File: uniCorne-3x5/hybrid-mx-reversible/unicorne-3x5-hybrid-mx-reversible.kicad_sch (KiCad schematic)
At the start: 87 parts, among them J1 MJ-4PP-9, J2 Nice!View, J3 Conn_01x02, J3 Conn_01x03, SW1 SW_MX_HS, SW10 SW_MX_HS, SW11 SW_MX_HS, SW12 SW_MX_HS, SW13 SW_MX_HS, SW14 SW_MX_HS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

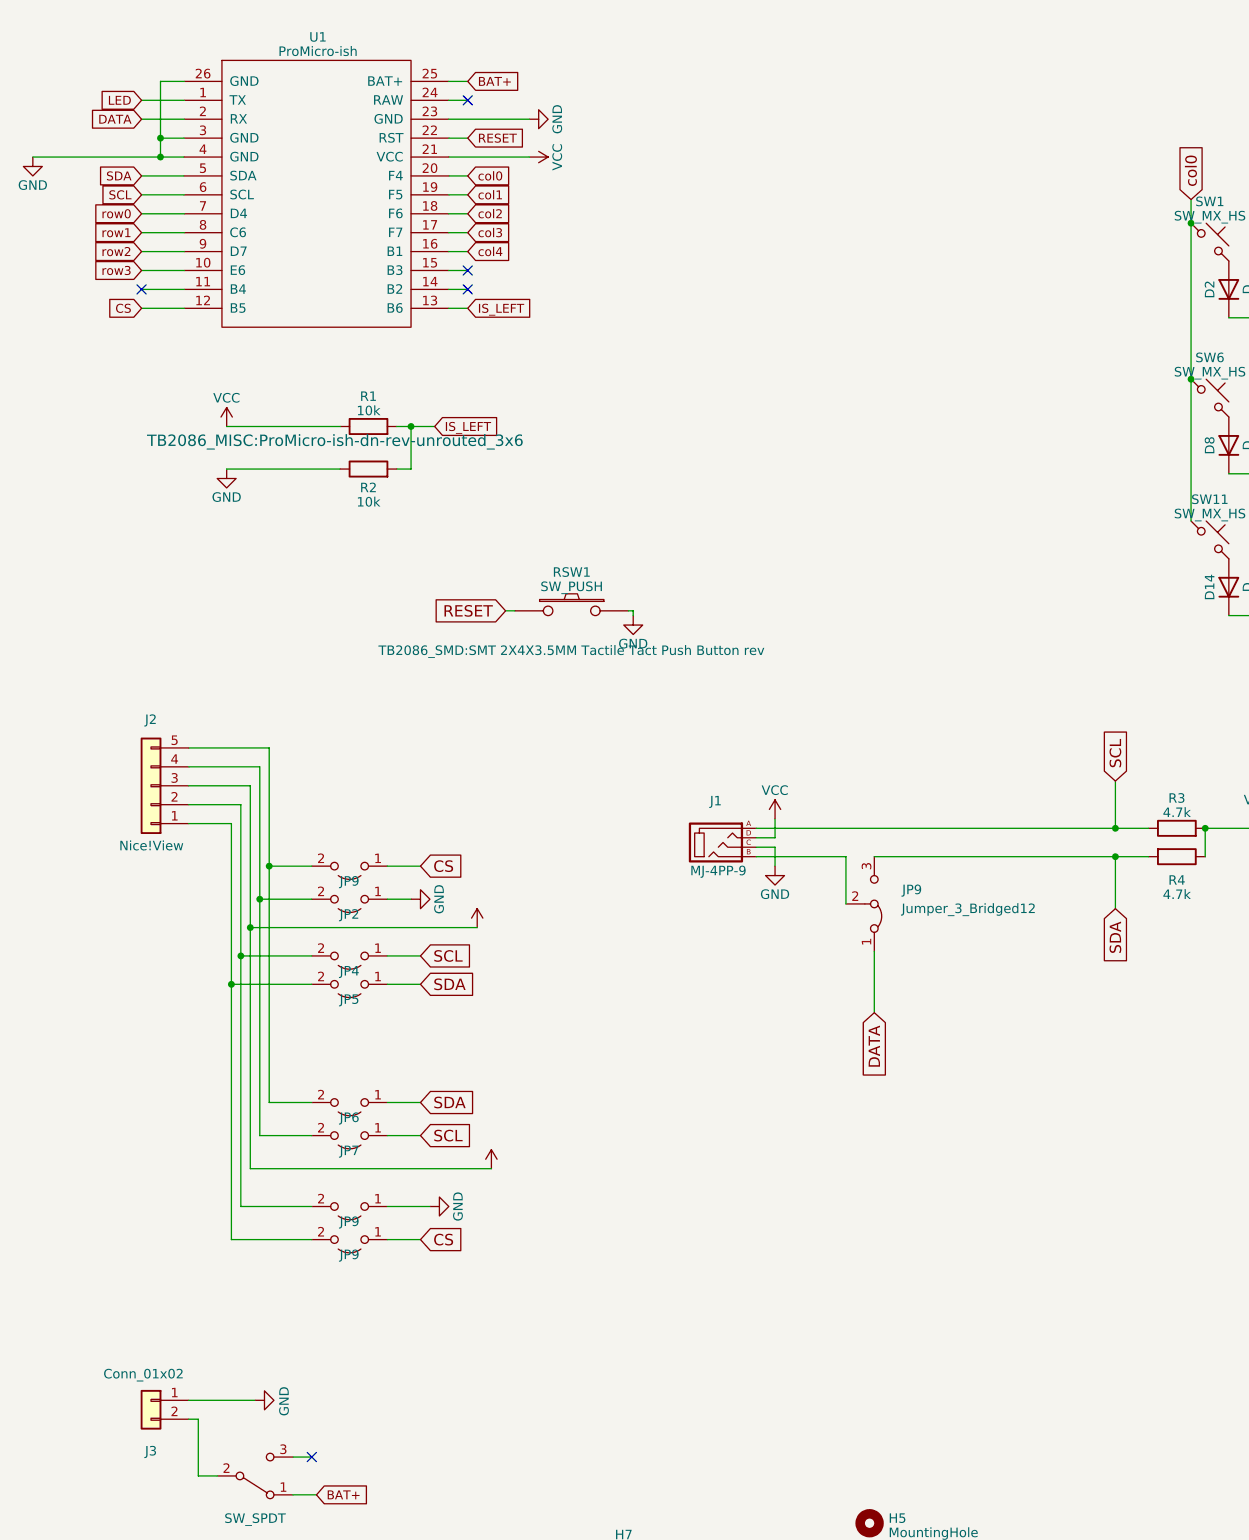
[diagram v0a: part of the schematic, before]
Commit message: fixed 3x5 hyprid mx
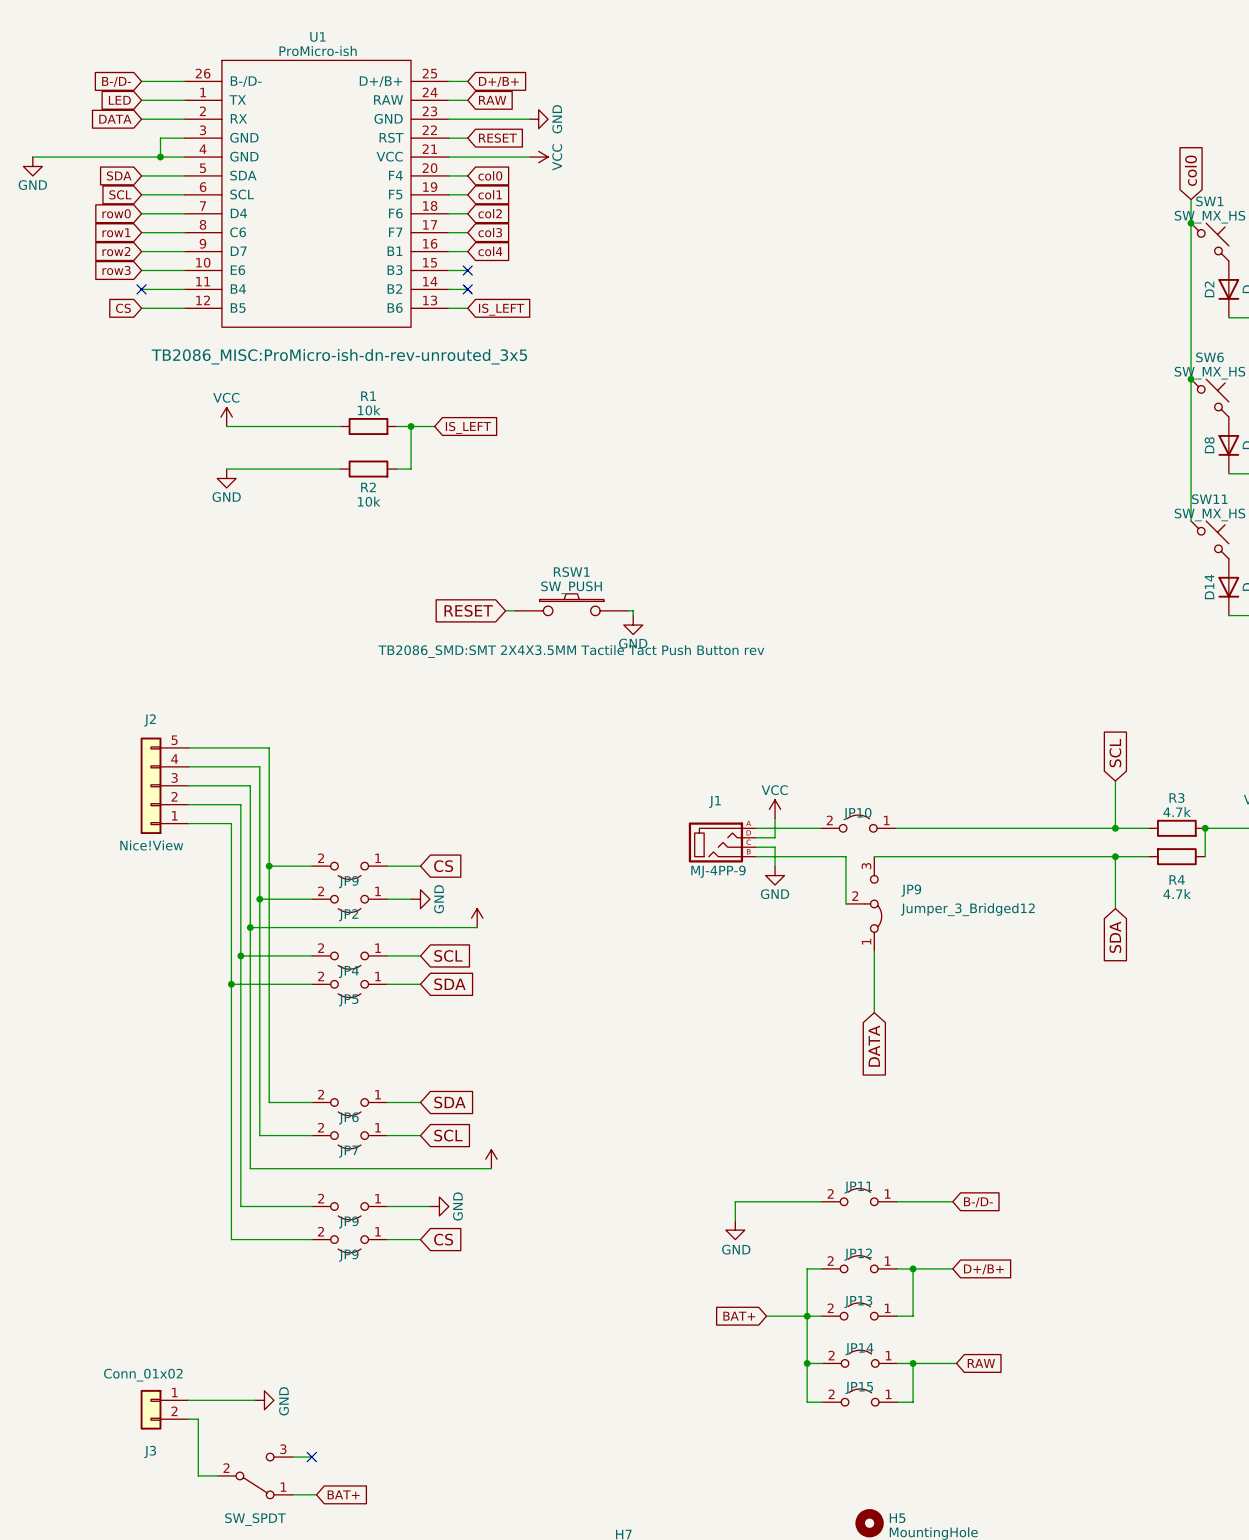
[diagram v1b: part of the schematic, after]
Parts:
- added JP10, JP11: (no value), TB2086_MISC:SolderJumper-2_P1.3mm_Open_TrianglePad1.0x1.2mm_rev, symbol Jumper:Jumper_2_Open
- added JP12, JP13, JP14, JP15: (no value), TB2086_MISC:SolderJumper-2_P1.3mm_Open_TrianglePad1.0x1.2mm, symbol Jumper:Jumper_2_Open
- U1: footprint TB2086_MISC:ProMicro-ish-dn-rev-unrouted_3x6 -> TB2086_MISC:ProMicro-ish-dn-rev-unrouted_3x5
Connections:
- net BAT+: now also JP12.2 (B), JP13.2 (B), JP14.2 (B), JP15.2 (B); no longer U1.25 (BAT+)
- net GND: now also JP11.2 (B); no longer U1.26 (GND)
- net SCL: now also JP10.1 (A); no longer J1.A
- net RAW: now reaches U1.24 (RAW)
- net RAW: now also JP14.1 (A), JP15.1 (A)
- new net: J1.A, JP10.2 (B)
- new net B-/D-: JP11.1 (A), U1.26 (B-/D-)
- new net D+/B+: JP12.1 (A), JP13.1 (A), U1.25 (D+/B+)
- no-connect marks 6 -> 5

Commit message: fixed 3x5
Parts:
- removed JP12, JP13, JP14, JP15: (no value), TB2086_MISC:SolderJumper-2_P1.3mm_Open_TrianglePad1.0x1.2mm, symbol Jumper:Jumper_2_Open
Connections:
- net D+/B+ is gone; now on net BAT+: U1.25 (D+/B+)
- net RAW is gone; now on net BAT+: U1.24 (RAW)
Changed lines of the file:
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@@
   (junction (at 200.66 55.88) (diameter 0) (color 0 0 0 0)
   )
-  (junction (at 126.238 189.992) (diameter 0) (color 0 0 0 0)
-  )
   (junction (at 361.95 217.17) (diameter 0) (color 0 0 0 0)
   )
@@
   (junction (at 307.34 198.12) (diameter 0) (color 0 0 0 0)
   )
-  (junction (at 140.462 196.342) (diameter 0) (color 0 0 0 0)
-  )
   (junction (at 370.84 109.22) (diameter 0) (color 0 0 0 0)
   )
@@
   (junction (at 213.36 43.18) (diameter 0) (color 0 0 0 0)
   )
-  (junction (at 126.238 196.342) (diameter 0) (color 0 0 0 0)
-  )
   (junction (at 361.95 198.12) (diameter 0) (color 0 0 0 0)
   )
@@
   )
   (junction (at 73.025 70.485) (diameter 0) (color 0 0 0 0)
-  )
-  (junction (at 140.462 183.642) (diameter 0) (color 0 0 0 0)
   )
   (junction (at 346.71 130.81) (diameter 0) (color 0 0 0 0)
@@
     (stroke (width 0) (type default))
   )
-  (wire (pts (xy 138.43 201.549) (xy 140.462 201.549))
-    (stroke (width 0) (type default))
-  )
   (wire (pts (xy 279.4 177.8) (xy 279.4 198.12))
     (stroke (width 0) (type default))
@@
     (stroke (width 0) (type default))
   )
-  (wire (pts (xy 126.238 189.992) (xy 128.143 189.992))
-    (stroke (width 0) (type default))
-  )
   (wire (pts (xy 269.24 217.17) (xy 279.4 217.17))
     (stroke (width 0) (type default))
@@
     (stroke (width 0) (type default))
   )
-  (wire (pts (xy 128.27 201.549) (xy 126.238 201.549))
-    (stroke (width 0) (type default))
-  )
   (wire (pts (xy 261.62 168.91) (xy 261.62 170.18))
     (stroke (width 0) (type default))
@@
     (stroke (width 0) (type default))
   )
-  (wire (pts (xy 138.303 189.992) (xy 140.462 189.992))
-    (stroke (width 0) (type default))
-  )
-  (wire (pts (xy 140.462 189.992) (xy 140.462 183.642))
-    (stroke (width 0) (type default))
-  )
-  (wire (pts (xy 126.238 183.642) (xy 126.238 189.992))
-    (stroke (width 0) (type default))
-  )
-  (wire (pts (xy 140.462 183.642) (xy 145.796 183.642))
-    (stroke (width 0) (type default))
-  )
   (wire (pts (xy 289.56 185.42) (xy 289.56 190.5))
     (stroke (width 0) (type default))
@@
     (stroke (width 0) (type default))
   )
-  (wire (pts (xy 126.238 183.642) (xy 128.143 183.642))
-    (stroke (width 0) (type default))
-  )
   (wire (pts (xy 279.4 177.8) (xy 281.94 177.8))
     (stroke (width 0) (type default))
@@
     (stroke (width 0) (type default))
   )
-  (wire (pts (xy 140.462 201.549) (xy 140.462 196.342))
-    (stroke (width 0) (type default))
-  )
-  (wire (pts (xy 120.777 189.992) (xy 126.238 189.992))
-    (stroke (width 0) (type default))
-  )
   (wire (pts (xy 53.975 161.29) (xy 59.69 161.29))
     (stroke (width 0) (type default))
@@
     (stroke (width 0) (type default))
   )
-  (wire (pts (xy 140.462 196.342) (xy 146.304 196.342))
-    (stroke (width 0) (type default))
-  )
   (wire (pts (xy 304.8 109.22) (xy 318.77 109.22))
     (stroke (width 0) (type default))
@@
     (stroke (width 0) (type default))
   )
-  (wire (pts (xy 126.238 196.342) (xy 126.238 189.992))
-    (stroke (width 0) (type default))
-  )
   (wire (pts (xy 361.95 198.12) (xy 363.22 198.12))
     (stroke (width 0) (type default))
   )
-  (wire (pts (xy 126.238 201.549) (xy 126.238 196.342))
-    (stroke (width 0) (type default))
-  )
   (wire (pts (xy 309.88 142.24) (xy 311.15 142.24))
     (stroke (width 0) (type default))
@@
     (stroke (width 0) (type default))
   )
-  (wire (pts (xy 138.303 183.642) (xy 140.462 183.642))
-    (stroke (width 0) (type default))
-  )
   (wire (pts (xy 138.303 174.625) (xy 145.796 174.625))
     (stroke (width 0) (type default))
@@
     (stroke (width 0) (type default))
   )
-  (wire (pts (xy 128.27 196.342) (xy 126.238 196.342))
-    (stroke (width 0) (type default))
-  )
   (wire (pts (xy 195.58 43.18) (xy 195.58 64.135))
     (stroke (width 0) (type default))
@@
   )
   (wire (pts (xy 396.24 142.24) (xy 378.46 142.24))
-    (stroke (width 0) (type default))
-  )
-  (wire (pts (xy 138.43 196.342) (xy 140.462 196.342))
     (stroke (width 0) (type default))
   )
@@
     )
   )
-  (global_label "BAT+" (shape input) (at 120.777 189.992 180) (fields_autoplaced)
-    (effects (font (size 1.1938 1.1938)) (justify right))
-    (property "Intersheetrefs" "${INTERSHEET_REFS}" (at 113.3666 189.992 0)
-      (effects (font (size 1.27 1.27)) (justify right) hide)
-    )
-  )
   (global_label "IS_LEFT" (shape input) (at 76.2 70.485 0) (fields_autoplaced)
     (effects (font (size 1.1938 1.1938)) (justify left))
@@
     )
   )
-  (global_label "D+{slash}B+" (shape input) (at 80.645 24.13 0) (fields_autoplaced)
+  (global_label "BAT+" (shape input) (at 80.645 24.13 0) (fields_autoplaced)
     (effects (font (size 1.1938 1.1938)) (justify left))
-    (property "Intersheetrefs" "${INTERSHEET_REFS}" (at 90.0449 24.13 0)
+    (property "Intersheetrefs" "${INTERSHEET_REFS}" (at 88.0554 24.13 0)
       (effects (font (size 1.27 1.27)) (justify left) hide)
     )
@@
     )
   )
-  (global_label "D+{slash}B+" (shape input) (at 145.796 183.642 0) (fields_autoplaced)
+  (global_label "BAT+" (shape input) (at 80.645 26.67 0) (fields_autoplaced)
     (effects (font (size 1.1938 1.1938)) (justify left))
-    (property "Intersheetrefs" "${INTERSHEET_REFS}" (at 155.1959 183.642 0)
-      (effects (font (size 1.27 1.27)) (justify left) hide)
-    )
-  )
-  (global_label "RAW" (shape input) (at 80.645 26.67 0) (fields_autoplaced)
-    (effects (font (size 1.1938 1.1938)) (justify left))
-    (property "Intersheetrefs" "${INTERSHEET_REFS}" (at 87.0321 26.67 0)
+    (property "Intersheetrefs" "${INTERSHEET_REFS}" (at 88.0554 26.67 0)
       (effects (font (size 1.27 1.27)) (justify left) hide)
     )
@@
     )
   )
-  (global_label "RAW" (shape input) (at 146.304 196.342 0) (fields_autoplaced)
-    (effects (font (size 1.1938 1.1938)) (justify left))
-    (property "Intersheetrefs" "${INTERSHEET_REFS}" (at 152.6911 196.342 0)
-      (effects (font (size 1.27 1.27)) (justify left) hide)
-    )
-  )
   (global_label "B-{slash}D-" (shape input) (at 145.796 174.625 0) (fields_autoplaced)
     (effects (font (size 1.1938 1.1938)) (justify left))
@@
     )
   )
-  (symbol (lib_id "Jumper:Jumper_2_Open") (at 133.223 183.642 0) (mirror y) (unit 1)
-    (in_bom yes) (on_board yes) (dnp no)
-    (property "Reference" "JP12" (at 133.223 181.61 0)
-      (effects (font (size 1.27 1.27)))
-    )
-    (property "Value" " " (at 132.969 185.166 0)
-      (effects (font (size 1.27 1.27)))
-    )
-    (property "Footprint" "TB2086_MISC:SolderJumper-2_P1.3mm_Open_TrianglePad1.0x1.2mm" (at 133.223 183.642 0)
-      (effects (font (size 1.27 1.27)) hide)
-    )
-    (property "Datasheet" "~" (at 133.223 183.642 0)
-      (effects (font (size 1.27 1.27)) hide)
-    )
-    (pin "1")
-    (pin "2")
-    (instances
-      (project "unicorne-3x5-hybrid-mx-reversible"
-        (path "/ea5c1f8d-7557-4cbf-a5a2-ee0a51c138e9"
-          (reference "JP12") (unit 1)
-        )
-      )
-    )
-  )
   (symbol (lib_id "Device:D") (at 218.44 111.76 90) (unit 1)
     (in_bom yes) (on_board yes) (dnp no)
@@
         (path "/ea5c1f8d-7557-4cbf-a5a2-ee0a51c138e9"
           (reference "JP4") (unit 1)
-        )
-      )
-    )
-  )
-  (symbol (lib_id "Jumper:Jumper_2_Open") (at 133.223 189.992 0) (mirror y) (unit 1)
-    (in_bom yes) (on_board yes) (dnp no)
-    (property "Reference" "JP13" (at 133.223 187.96 0)
-      (effects (font (size 1.27 1.27)))
-    )
-    (property "Value" " " (at 132.969 191.516 0)
-      (effects (font (size 1.27 1.27)))
-    )
-    (property "Footprint" "TB2086_MISC:SolderJumper-2_P1.3mm_Open_TrianglePad1.0x1.2mm" (at 133.223 189.992 0)
-      (effects (font (size 1.27 1.27)) hide)
-    )
-    (property "Datasheet" "~" (at 133.223 189.992 0)
-      (effects (font (size 1.27 1.27)) hide)
-    )
-    (pin "1")
-    (pin "2")
-    (instances
-      (project "unicorne-3x5-hybrid-mx-reversible"
-        (path "/ea5c1f8d-7557-4cbf-a5a2-ee0a51c138e9"
-          (reference "JP13") (unit 1)
         )
       )
@@
     )
   )
-  (symbol (lib_id "Jumper:Jumper_2_Open") (at 133.35 201.549 0) (mirror y) (unit 1)
-    (in_bom yes) (on_board yes) (dnp no)
-    (property "Reference" "JP15" (at 133.35 199.517 0)
-      (effects (font (size 1.27 1.27)))
-    )
-    (property "Value" " " (at 133.096 203.073 0)
-      (effects (font (size 1.27 1.27)))
-    )
-    (property "Footprint" "TB2086_MISC:SolderJumper-2_P1.3mm_Open_TrianglePad1.0x1.2mm" (at 133.35 201.549 0)
-      (effects (font (size 1.27 1.27)) hide)
-    )
-    (property "Datasheet" "~" (at 133.35 201.549 0)
-      (effects (font (size 1.27 1.27)) hide)
-    )
-    (pin "1")
-    (pin "2")
-    (instances
-      (project "unicorne-3x5-hybrid-mx-reversible"
-        (path "/ea5c1f8d-7557-4cbf-a5a2-ee0a51c138e9"
-          (reference "JP15") (unit 1)
-        )
-      )
-    )
-  )
   (symbol (lib_id "power:GND") (at 22.225 34.29 0) (unit 1)
     (in_bom yes) (on_board yes) (dnp no)
@@
         )
       )
-    )
-  )
-  (symbol (lib_id "Jumper:Jumper_2_Open") (at 133.35 196.342 0) (mirror y) (unit 1)
-    (in_bom yes) (on_board yes) (dnp no)
-    (property "Reference" "JP14" (at 133.35 194.31 0)
-      (effects (font (size 1.27 1.27)))
-    )
-    (property "Value" " " (at 133.096 197.866 0)
-      (effects (font (size 1.27 1.27)))
-    )
-    (property "Footprint" "TB2086_MISC:SolderJumper-2_P1.3mm_Open_TrianglePad1.0x1.2mm" (at 133.35 196.342 0)
-      (effects (font (size 1.27 1.27)) hide)
-    )
-    (property "Datasheet" "~" (at 133.35 196.342 0)
-      (effects (font (size 1.27 1.27)) hide)
-    )
-    (pin "1")
-    (pin "2")
-    (instances
-      (project "unicorne-3x5-hybrid-mx-reversible"
-        (path "/ea5c1f8d-7557-4cbf-a5a2-ee0a51c138e9"
-          (reference "JP14") (unit 1)
-        )
-      )
